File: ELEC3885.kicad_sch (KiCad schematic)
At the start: 4 parts

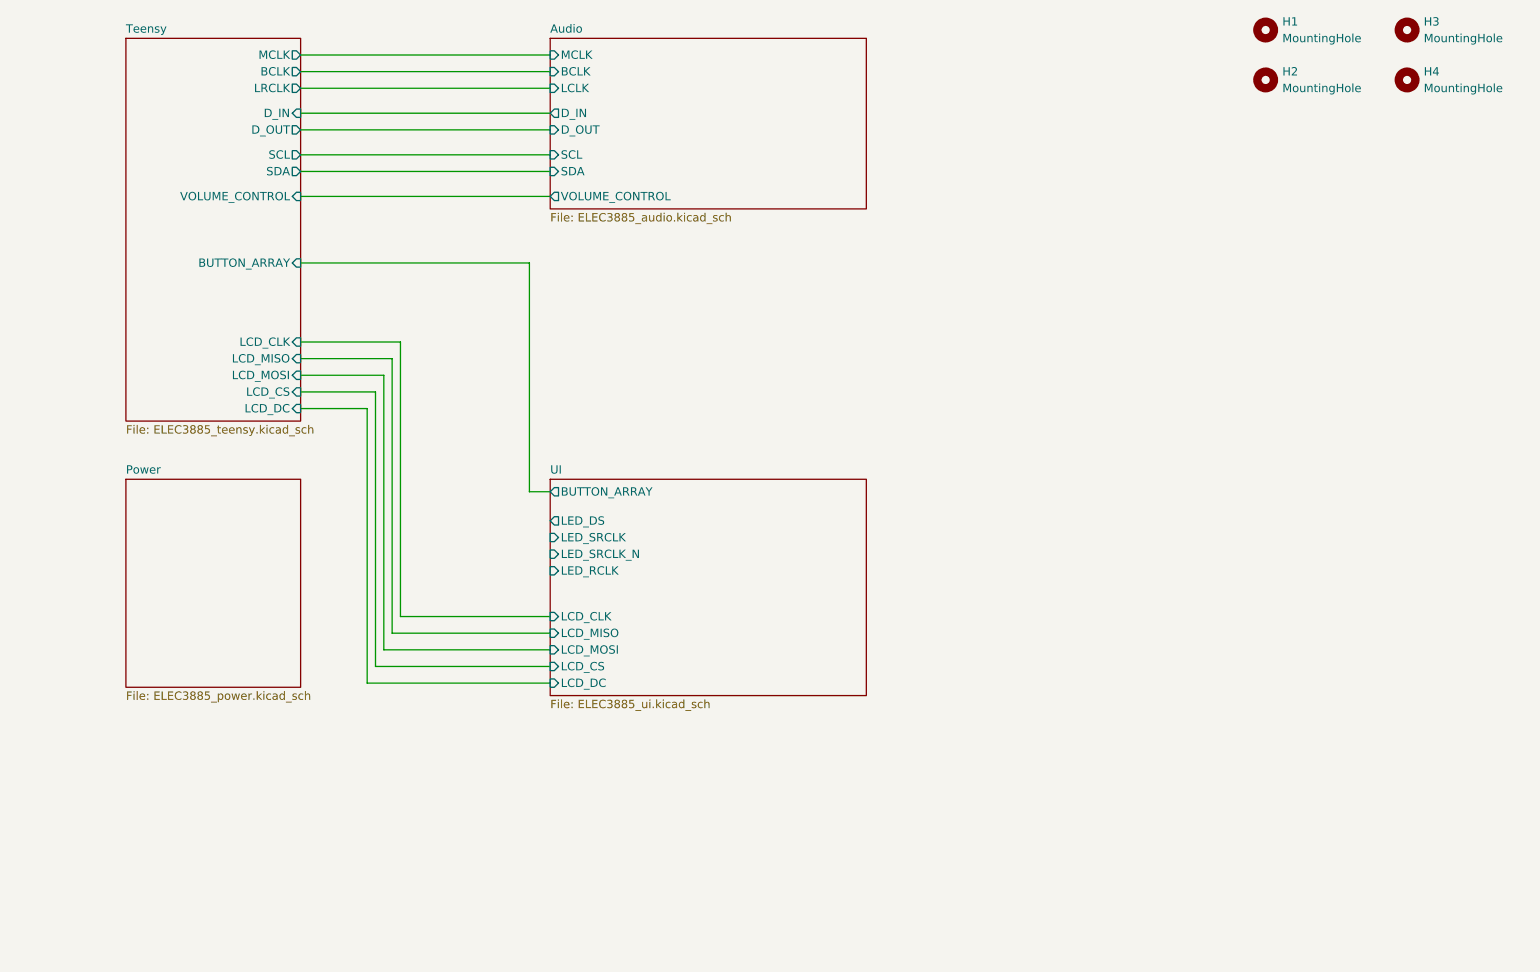
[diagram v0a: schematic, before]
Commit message: Rev3 rework, diff amp jumpers added
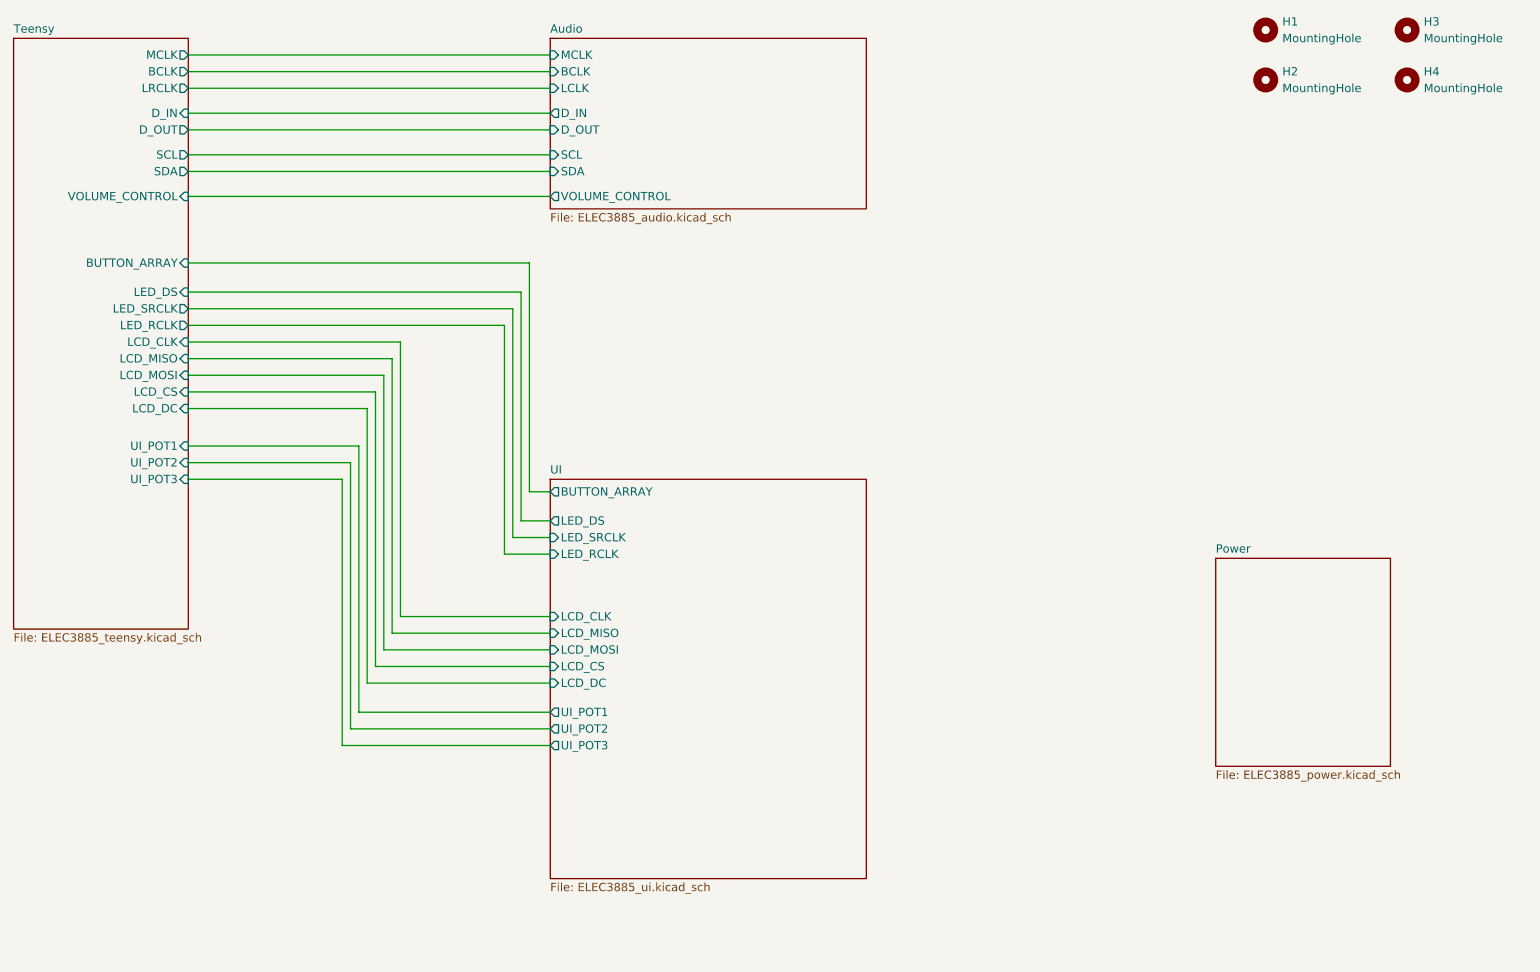
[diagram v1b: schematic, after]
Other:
- sheet Teensy ports: added LED_DS, LED_RCLK, LED_SRCLK, UI_POT1, UI_POT2, UI_POT3; removed none
- sheet UI ports: added UI_POT1, UI_POT2, UI_POT3; removed LED_SRCLK_N

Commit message: Encoders, RGB LED added, PCB cleanup
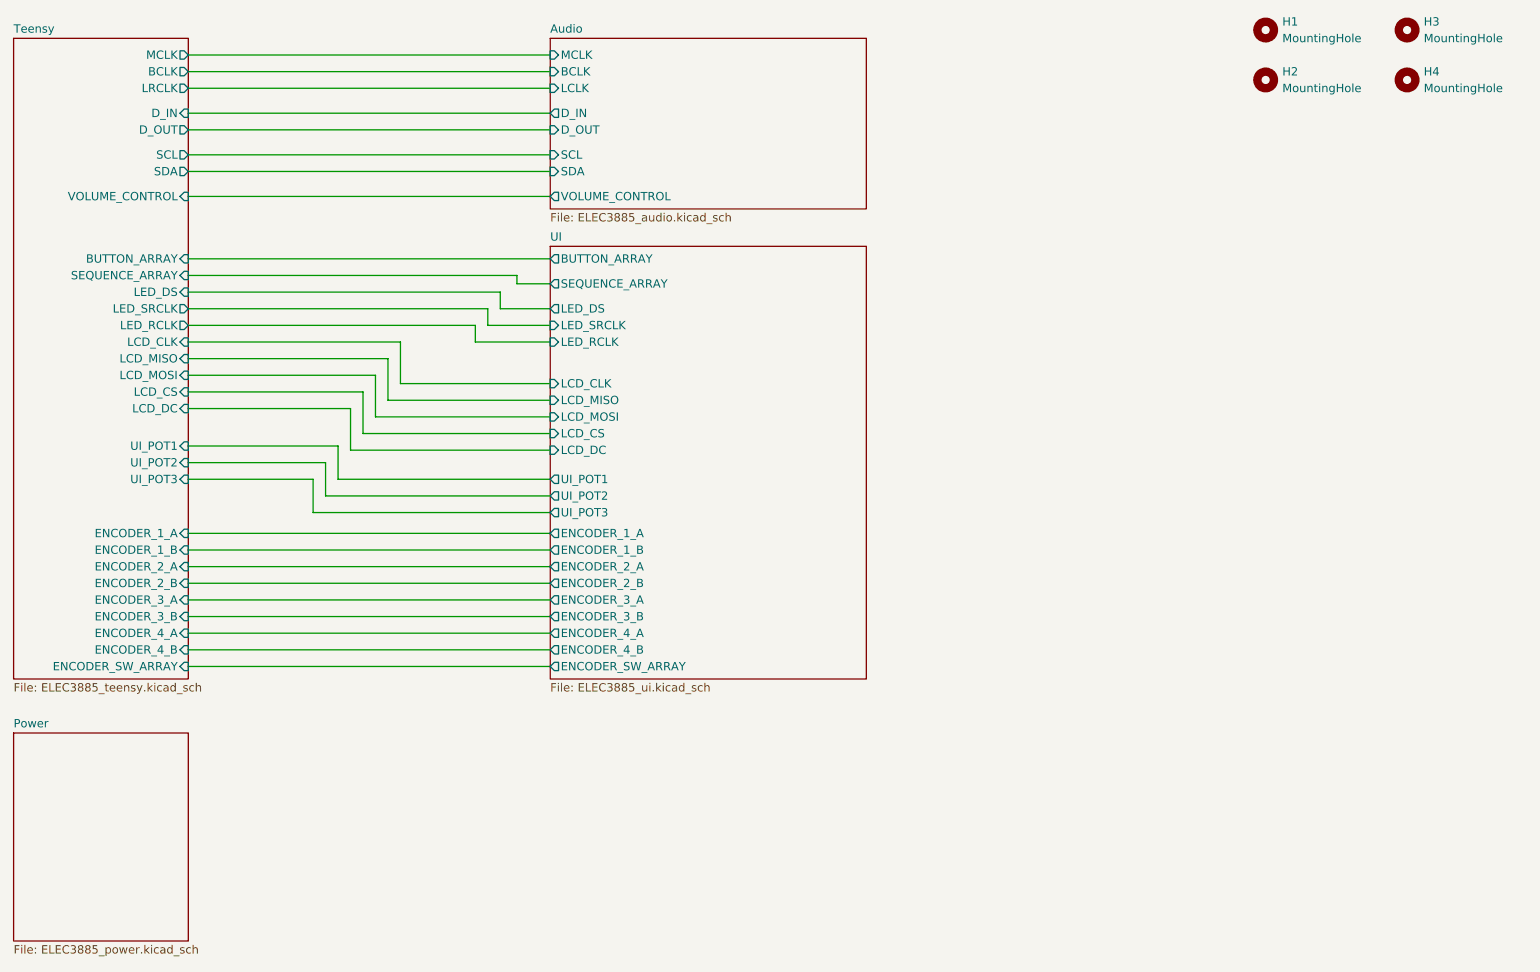
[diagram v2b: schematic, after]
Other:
- sheet Teensy ports: added ENCODER_1_A, ENCODER_1_B, ENCODER_2_A, ENCODER_2_B, ENCODER_3_A, ENCODER_3_B, ENCODER_4_A, ENCODER_4_B, ENCODER_SW_ARRAY, SEQUENCE_ARRAY; removed none
- sheet UI ports: added ENCODER_1_A, ENCODER_1_B, ENCODER_2_A, ENCODER_2_B, ENCODER_3_A, ENCODER_3_B, ENCODER_4_A, ENCODER_4_B, ENCODER_SW_ARRAY, SEQUENCE_ARRAY; removed none

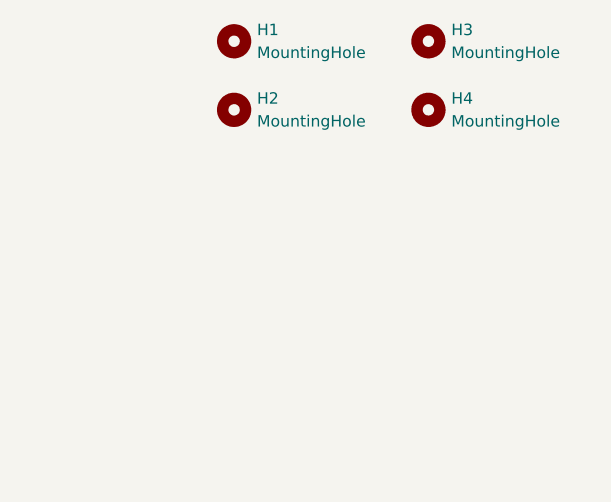
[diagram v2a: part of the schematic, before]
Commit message: Testpoints added, silkscreen cleaned
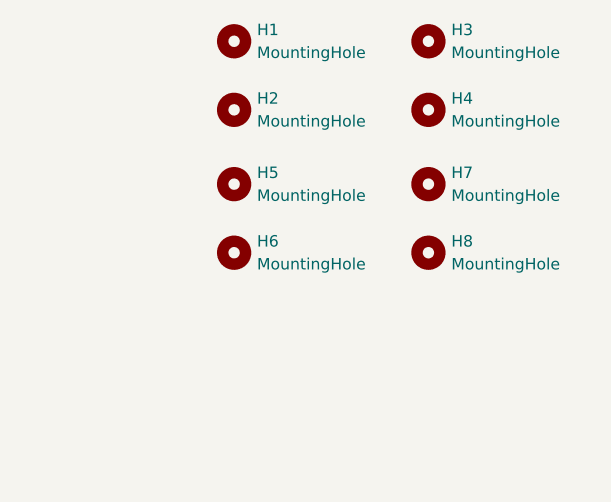
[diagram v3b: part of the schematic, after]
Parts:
- added H5, H6, H7, H8: MountingHole, MountingHole:MountingHole_3.2mm_M3, symbol Mechanical:MountingHole
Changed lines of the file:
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@@
     (stroke (width 0) (type default))
+  )
+  (symbol (lib_id "Mechanical:MountingHole") (at 246.38 48.895 0) (unit 1)
+    (in_bom yes) (on_board yes) (dnp no) (fields_autoplaced)
+    (property "Reference" "H7" (at 248.92 47.6249 0)
+      (effects (font (size 1.27 1.27)) (justify left))
+    )
+    (property "Value" "MountingHole" (at 248.92 50.1649 0)
+      (effects (font (size 1.27 1.27)) (justify left))
+    )
+    (property "Footprint" "MountingHole:MountingHole_3.2mm_M3" (at 246.38 48.895 0)
+      (effects (font (size 1.27 1.27)) hide)
+    )
+    (property "Datasheet" "~" (at 246.38 48.895 0)
+      (effects (font (size 1.27 1.27)) hide)
+    )
+    (instances
+      (project "ELEC3885"
+        (path "/eaef1172-3351-417c-bfc4-74a598f141cb"
+          (reference "H7") (unit 1)
+        )
+      )
+    )
+  )
+  (symbol (lib_id "Mechanical:MountingHole") (at 246.38 56.515 0) (unit 1)
+    (in_bom yes) (on_board yes) (dnp no) (fields_autoplaced)
+    (property "Reference" "H8" (at 248.92 55.2449 0)
+      (effects (font (size 1.27 1.27)) (justify left))
+    )
+    (property "Value" "MountingHole" (at 248.92 57.7849 0)
+      (effects (font (size 1.27 1.27)) (justify left))
+    )
+    (property "Footprint" "MountingHole:MountingHole_3.2mm_M3" (at 246.38 56.515 0)
+      (effects (font (size 1.27 1.27)) hide)
+    )
+    (property "Datasheet" "~" (at 246.38 56.515 0)
+      (effects (font (size 1.27 1.27)) hide)
+    )
+    (instances
+      (project "ELEC3885"
+        (path "/eaef1172-3351-417c-bfc4-74a598f141cb"
+          (reference "H8") (unit 1)
+        )
+      )
+    )
+  )
+  (symbol (lib_id "Mechanical:MountingHole") (at 224.79 56.515 0) (unit 1)
+    (in_bom yes) (on_board yes) (dnp no) (fields_autoplaced)
+    (property "Reference" "H6" (at 227.33 55.2449 0)
+      (effects (font (size 1.27 1.27)) (justify left))
+    )
+    (property "Value" "MountingHole" (at 227.33 57.7849 0)
+      (effects (font (size 1.27 1.27)) (justify left))
+    )
+    (property "Footprint" "MountingHole:MountingHole_3.2mm_M3" (at 224.79 56.515 0)
+      (effects (font (size 1.27 1.27)) hide)
+    )
+    (property "Datasheet" "~" (at 224.79 56.515 0)
+      (effects (font (size 1.27 1.27)) hide)
+    )
+    (instances
+      (project "ELEC3885"
+        (path "/eaef1172-3351-417c-bfc4-74a598f141cb"
+          (reference "H6") (unit 1)
+        )
+      )
+    )
   )
   (symbol (lib_id "Mechanical:MountingHole") (at 246.38 33.02 0) (unit 1)
@@
         )
       )
+    )
+  )
+  (symbol (lib_id "Mechanical:MountingHole") (at 224.79 48.895 0) (unit 1)
+    (in_bom yes) (on_board yes) (dnp no) (fields_autoplaced)
+    (property "Reference" "H5" (at 227.33 47.6249 0)
+      (effects (font (size 1.27 1.27)) (justify left))
+    )
+    (property "Value" "MountingHole" (at 227.33 50.1649 0)
+      (effects (font (size 1.27 1.27)) (justify left))
+    )
+    (property "Footprint" "MountingHole:MountingHole_3.2mm_M3" (at 224.79 48.895 0)
+      (effects (font (size 1.27 1.27)) hide)
+    )
+    (property "Datasheet" "~" (at 224.79 48.895 0)
+      (effects (font (size 1.27 1.27)) hide)
+    )
+    (instances
+      (project "ELEC3885"
+        (path "/eaef1172-3351-417c-bfc4-74a598f141cb"
+          (reference "H5") (unit 1)
+        )
+      )
